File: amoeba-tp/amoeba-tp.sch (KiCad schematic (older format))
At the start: 34 parts

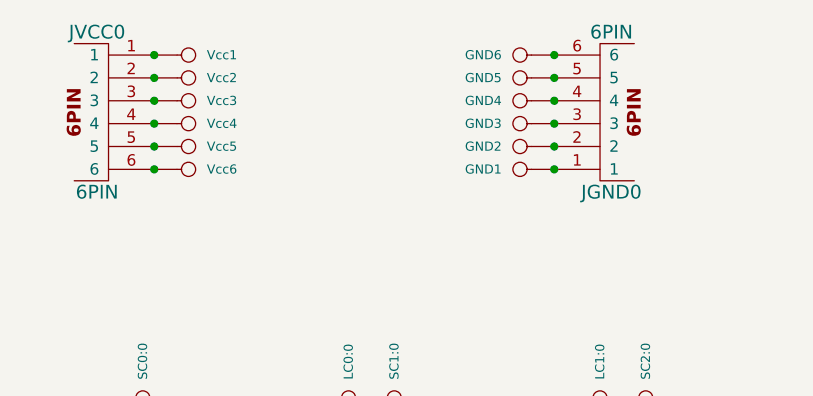
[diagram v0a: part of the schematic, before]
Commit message: Added fill zones.
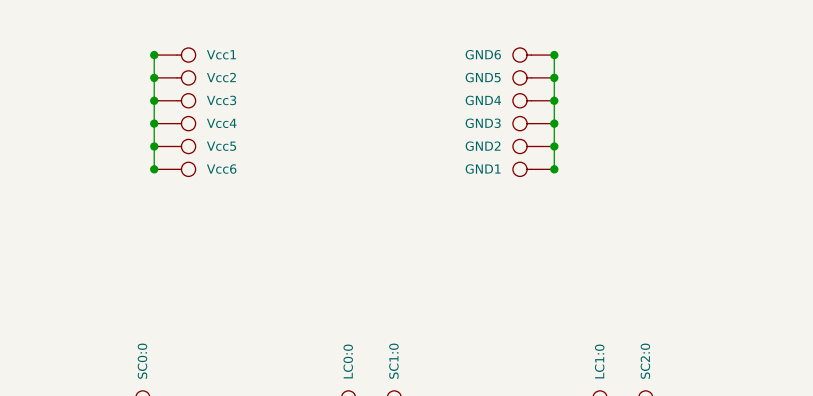
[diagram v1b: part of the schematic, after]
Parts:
- removed JGND0, JVCC0: 6PIN, ~, symbol 6PIN
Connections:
- net at Vcc1.1: now also Vcc2.1, Vcc3.1, Vcc4.1, Vcc5.1, Vcc6.1
- net at GND1.1: now also GND2.1, GND3.1, GND4.1, GND5.1, GND6.1
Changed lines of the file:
@@
 Connection ~ 4100 3450
 Connection ~ 4100 3050
-$Comp
-L 6PIN JVCC0
-U 1 1 55D7F9DE
-P 4050 1400
-F 0 "JVCC0" H 4000 1750 60  0000 C CNN
-F 1 "6PIN" H 4000 1050 60  0000 C CNN
-F 2 "~" H 4050 1400 60  0000 C CNN
-F 3 "~" H 4050 1400 60  0000 C CNN
-	1    4050 1400
-	1    0    0    -1
-$EndComp
-$Comp
-L 6PIN JGND0
-U 1 1 55D7FA7E
-P 6200 1400
-F 0 "JGND0" H 6150 1750 60  0000 C CNN
-F 1 "6PIN" H 6150 1050 60  0000 C CNN
-F 2 "~" H 6200 1400 60  0000 C CNN
-F 3 "~" H 6200 1400 60  0000 C CNN
-	1    6200 1400
-	-1   0    0    1
-$EndComp
 Connection ~ 6000 1550
 Connection ~ 6000 1450
@@
 	-1   0    0    1
 $EndComp
+Wire Wire Line
+	6000 1150 6000 1650
+Wire Wire Line
+	4250 1150 4250 1650
 $EndSCHEMATC

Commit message: Cleaned up Amoeba TP design.
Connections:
- net key0:0/LC0 renamed key:H/LC0
- net key0:0/LR0 renamed key:H/LR0
- net key0:0/SC0 renamed key:H/SC0
- net key0:0/SR0 renamed key:H/SR0
- net key0:1/LC1 renamed key:N/LC1
- net key0:1/LR0 renamed key:N/LR0
- net key0:1/SC1 renamed key:N/SC1
- net key0:1/SR0 renamed key:N/SR0
- net key1:0/LC0 renamed key:G/LC0
- net key1:0/LR1 renamed key:G/LR1
- net key1:0/SC0 renamed key:G/SC0
- net key1:0/SR1 renamed key:G/SR1
- net key1:1/LC1 renamed key:B/LC1
- net key1:1/SC1 renamed key:B/SC1
- net key2:1/LC0 renamed key:V/LC0
- net key2:1/LC1 renamed key:V/LC1
- net key2:1/LR1 renamed key:V/LR1
- net key2:1/SC0 renamed key:V/SC0
- net key2:1/SC1 renamed key:V/SC1
- net key2:1/SR1 renamed key:V/SR1
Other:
- moved on the sheet: GND1, GND2, GND3, GND4, GND5, GND6, LC0:0, LC0:1, LC1:0, LC1:1, LC2:0, LC2:1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
